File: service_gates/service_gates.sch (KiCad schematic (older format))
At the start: 1 part, among them P1 DIN_41612_128P

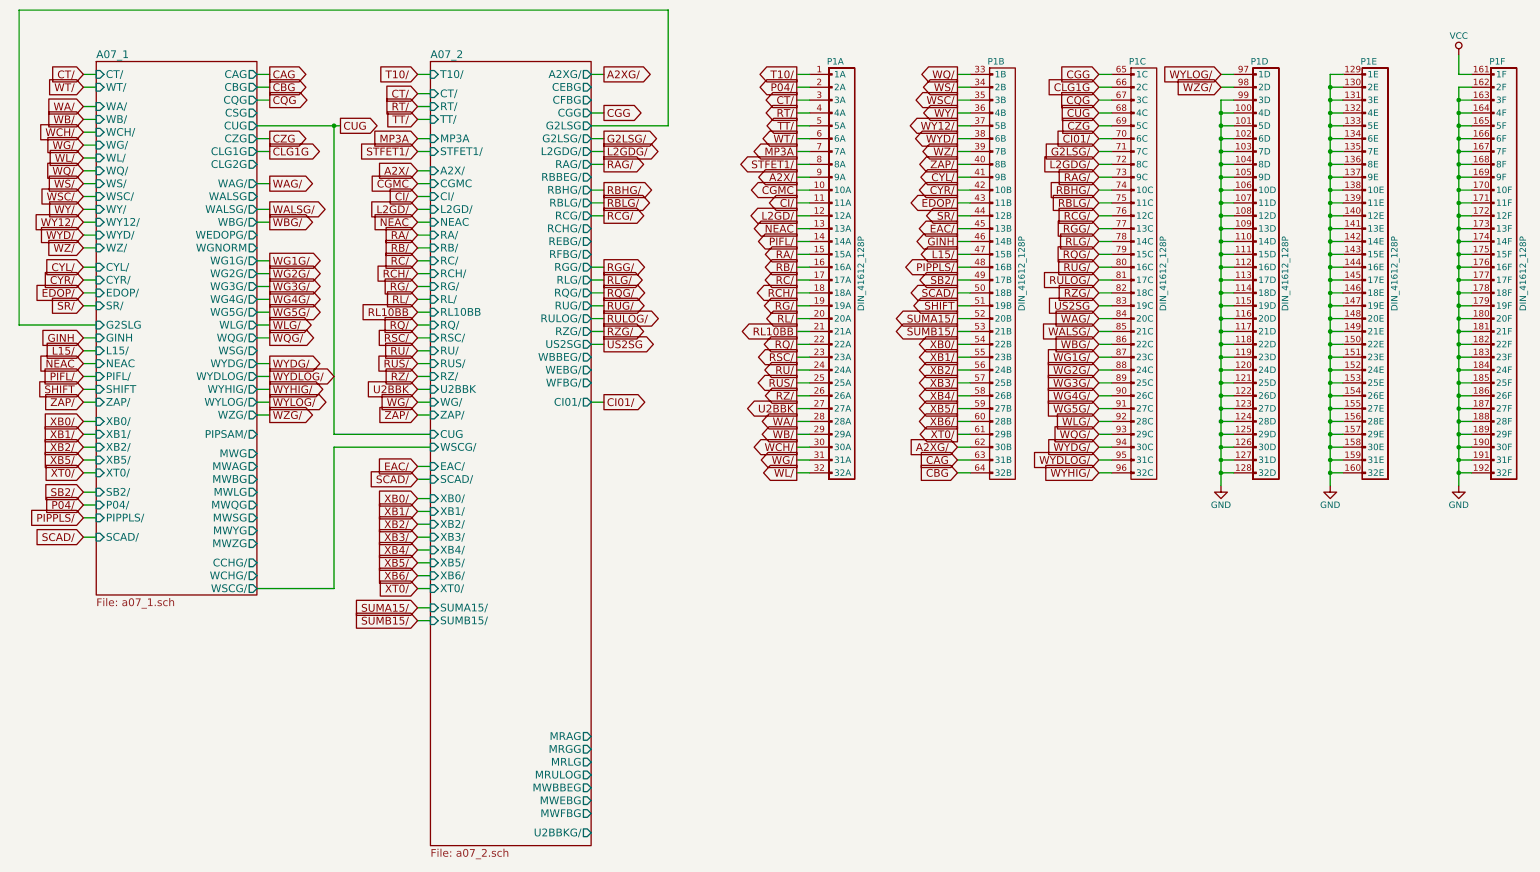
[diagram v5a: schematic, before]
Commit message: Added and tied in module 12, parity & s register
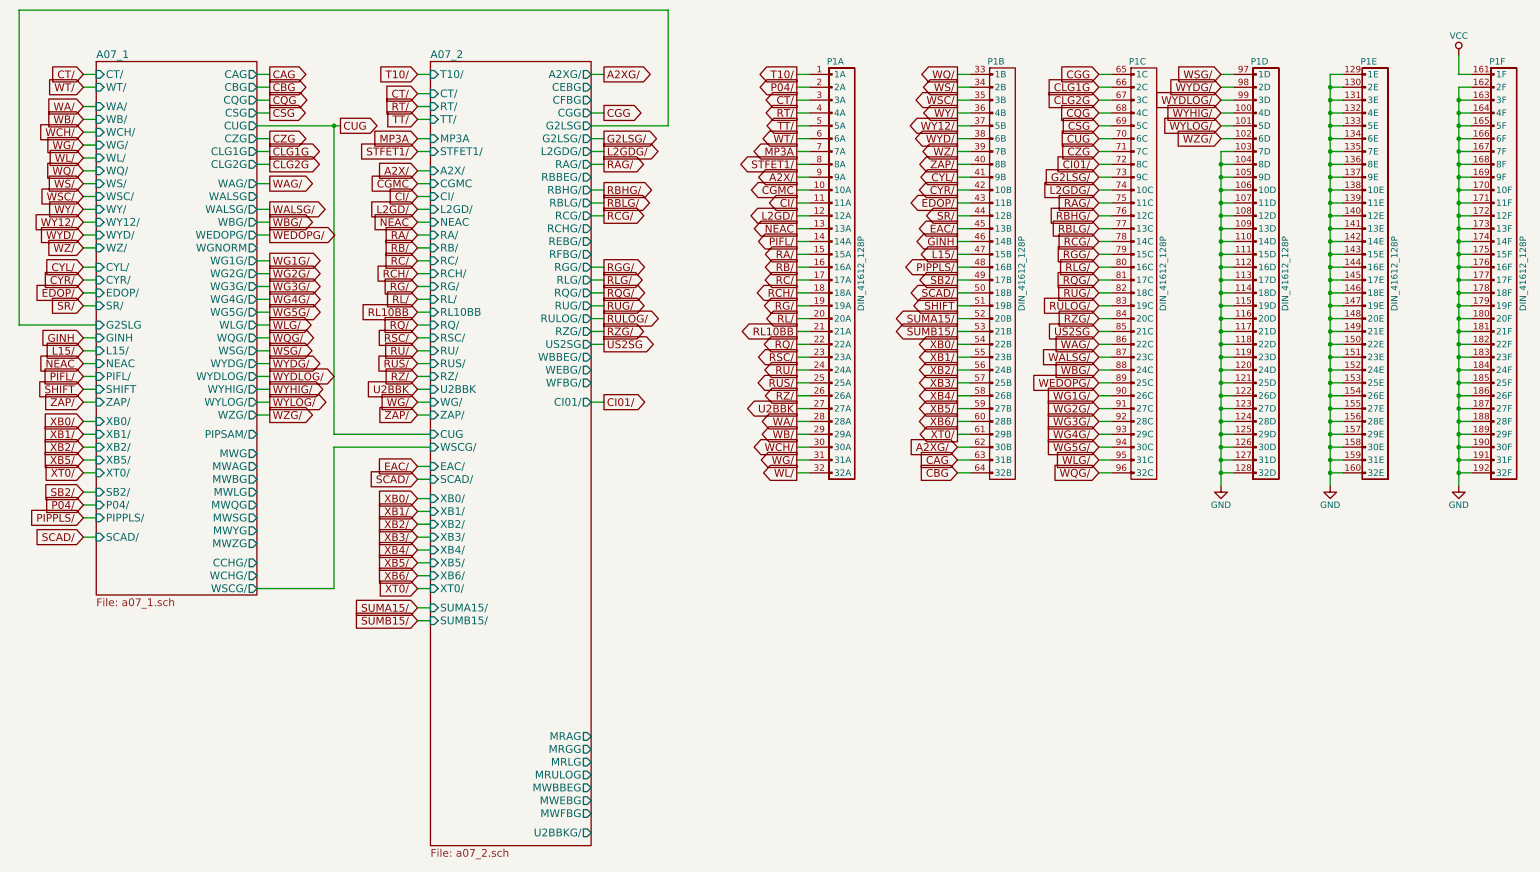
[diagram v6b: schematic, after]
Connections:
- net CI01/: now also P1.72 (8C); no longer P1.70 (6C)
- net CQG: now also P1.68 (4C); no longer P1.67 (3C)
- net CUG: now also P1.70 (6C); no longer P1.68 (4C)
- net CZG: now also P1.71 (7C); no longer P1.69 (5C)
- net G2LSG/: now also P1.73 (9C); no longer P1.71 (7C)
- net GND: no longer P1.100 (4D), P1.101 (5D), P1.102 (6D), P1.99 (3D)
- net L2GDG/: now also P1.74 (10C); no longer P1.72 (8C)
- net RAG/: now also P1.75 (11C); no longer P1.73 (9C)
- net RBHG/: now also P1.76 (12C); no longer P1.74 (10C)
- net RBLG/: now also P1.77 (13C); no longer P1.75 (11C)
- net RCG/: now also P1.78 (14C); no longer P1.76 (12C)
- net RGG/: now also P1.79 (15C); no longer P1.77 (13C)
- net RLG/: now also P1.80 (16C); no longer P1.78 (14C)
- net RQG/: now also P1.81 (17C); no longer P1.79 (15C)
- net RUG/: now also P1.82 (18C); no longer P1.80 (16C)
- net RULOG/: now also P1.83 (19C); no longer P1.81 (17C)
- net RZG/: now also P1.84 (20C); no longer P1.82 (18C)
- net US2SG: now also P1.85 (21C); no longer P1.83 (19C)
- net WAG/: now also P1.86 (22C); no longer P1.84 (20C)
- net WALSG/: now also P1.87 (23C); no longer P1.85 (21C)
- net WBG/: now also P1.88 (24C); no longer P1.86 (22C)
- net WG1G/: now also P1.90 (26C); no longer P1.87 (23C)
- net WG2G/: now also P1.91 (27C); no longer P1.88 (24C)
- net WG3G/: now also P1.92 (28C); no longer P1.89 (25C)
- net WG4G/: now also P1.93 (29C); no longer P1.90 (26C)
- net WG5G/: now also P1.94 (30C); no longer P1.91 (27C)
- net WLG/: now also P1.95 (31C); no longer P1.92 (28C)
- net WQG/: now also P1.96 (32C); no longer P1.93 (29C)
- net WYDG/: now also P1.98 (2D); no longer P1.94 (30C)
- net WYDLOG/: now also P1.99 (3D); no longer P1.95 (31C)
- net WYHIG/: now also P1.100 (4D); no longer P1.96 (32C)
- net WYLOG/: now also P1.101 (5D); no longer P1.97 (1D)
- net WZG/: now also P1.102 (6D); no longer P1.98 (2D)
- new net CLG2G: P1.67 (3C)
- new net CSG: P1.69 (5C)
- new net WEDOPG/: P1.89 (25C)
- new net WSG/: P1.97 (1D)
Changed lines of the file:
@@
 $EndComp
 Wire Wire Line
-	11550 1450 11650 1450
-Wire Wire Line
-	10600 3050 10700 3050
+	11550 1850 11650 1850
+Wire Wire Line
+	10600 3250 10700 3250
+Wire Wire Line
+	10600 2950 10700 2950
+Wire Wire Line
+	10600 2850 10700 2850
 Wire Wire Line
 	10600 2750 10700 2750
 Wire Wire Line
 	10600 2650 10700 2650
-Wire Wire Line
-	10600 2550 10700 2550
-Wire Wire Line
-	10600 2450 10700 2450
 $Comp
 L DIN_41612_128P P1
@@
 	11550 1950 11650 1950
 Connection ~ 11550 2050
-Wire Wire Line
-	11550 1850 11650 1850
-Connection ~ 11550 1950
-Wire Wire Line
-	11550 1750 11650 1750
-Connection ~ 11550 1850
-Wire Wire Line
-	11550 1650 11650 1650
-Connection ~ 11550 1750
-Wire Wire Line
-	11550 1550 11650 1550
-Connection ~ 11550 1650
 $Comp
 L DIN_41612_128P P1
@@
 Connection ~ 12400 1450
 Wire Wire Line
-	10600 1850 10700 1850
+	10600 2050 10700 2050
 $Sheet
 S 5400 1250 1250 6100
@@
 Connection ~ 4650 1750
 Wire Wire Line
-	10700 1550 10600 1550
-Text GLabel 10600 1550 0    60   Input ~ 0
-CQG
-Wire Wire Line
 	10700 1650 10600 1650
 Text GLabel 10600 1650 0    60   Input ~ 0
+CQG
+Wire Wire Line
+	10700 1850 10600 1850
+Text GLabel 10600 1850 0    60   Input ~ 0
 CUG
 Wire Wire Line
@@
 CZG
 Wire Wire Line
-	10700 1750 10600 1750
-Text GLabel 10600 1750 0    60   Input ~ 0
+	10700 1950 10600 1950
+Text GLabel 10600 1950 0    60   Input ~ 0
 CZG
 Wire Wire Line
@@
 Text GLabel 6750 3900 2    60   Output ~ 0
 CI01/
-Text GLabel 10600 1850 0    60   Input ~ 0
+Text GLabel 10600 2050 0    60   Input ~ 0
 CI01/
 Wire Wire Line
@@
 G2LSG/
 Wire Wire Line
-	10600 1950 10700 1950
-Text GLabel 10600 1950 0    60   Input ~ 0
+	10600 2150 10700 2150
+Text GLabel 10600 2150 0    60   Input ~ 0
 G2LSG/
 Wire Wire Line
@@
 L2GDG/
 Wire Wire Line
-	10600 2050 10700 2050
-Text GLabel 10600 2050 0    60   Input ~ 0
+	10600 2250 10700 2250
+Text GLabel 10600 2250 0    60   Input ~ 0
 L2GDG/
 Wire Wire Line
@@
 RAG/
 Wire Wire Line
-	10600 2150 10700 2150
-Text GLabel 10600 2150 0    60   Input ~ 0
+	10600 2350 10700 2350
+Text GLabel 10600 2350 0    60   Input ~ 0
 RAG/
 Wire Wire Line
@@
 RBLG/
 Wire Wire Line
-	10600 2350 10700 2350
-Text GLabel 10600 2350 0    60   Input ~ 0
+	10600 2550 10700 2550
+Text GLabel 10600 2550 0    60   Input ~ 0
 RBLG/
 Wire Wire Line
@@
 Text GLabel 6750 2450 2    60   Output ~ 0
 RCG/
-Text GLabel 10600 2450 0    60   Input ~ 0
+Text GLabel 10600 2650 0    60   Input ~ 0
 RCG/
 Wire Wire Line
@@
 Text GLabel 6750 2850 2    60   Output ~ 0
 RGG/
-Text GLabel 10600 2550 0    60   Input ~ 0
+Text GLabel 10600 2750 0    60   Input ~ 0
 RGG/
 Wire Wire Line
@@
 Text GLabel 6750 2950 2    60   Output ~ 0
 RLG/
-Text GLabel 10600 2650 0    60   Input ~ 0
+Text GLabel 10600 2850 0    60   Input ~ 0
 RLG/
 Wire Wire Line
@@
 Text GLabel 6750 3050 2    60   Output ~ 0
 RQG/
-Text GLabel 10600 2750 0    60   Input ~ 0
+Text GLabel 10600 2950 0    60   Input ~ 0
 RQG/
 Wire Wire Line
@@
 RULOG/
 Wire Wire Line
-	10600 2950 10700 2950
-Text GLabel 10600 2950 0    60   Input ~ 0
+	10600 3150 10700 3150
+Text GLabel 10600 3150 0    60   Input ~ 0
 RULOG/
 Wire Wire Line
@@
 Text GLabel 6750 3350 2    60   Output ~ 0
 RZG/
-Text GLabel 10600 3050 0    60   Input ~ 0
+Text GLabel 10600 3250 0    60   Input ~ 0
 RZG/
 Wire Wire Line
@@
 WALSG/
 Wire Wire Line
-	10600 3250 10700 3250
-Text GLabel 10600 3250 0    60   Input ~ 0
+	10600 3450 10700 3450
+Text GLabel 10600 3450 0    60   Input ~ 0
 WAG/
 Wire Wire Line
-	10600 3350 10700 3350
-Text GLabel 10600 3350 0    60   Input ~ 0
+	10600 3550 10700 3550
+Text GLabel 10600 3550 0    60   Input ~ 0
 WALSG/
 Wire Wire Line
@@
 WBG/
 Wire Wire Line
-	10600 3450 10700 3450
-Text GLabel 10600 3450 0    60   Input ~ 0
+	10600 3650 10700 3650
+Text GLabel 10600 3650 0    60   Input ~ 0
 WBG/
 Wire Wire Line
@@
 WG4G/
 Wire Wire Line
-	10600 3550 10700 3550
-Text GLabel 10600 3550 0    60   Input ~ 0
-WG1G/
-Wire Wire Line
-	10600 3750 10700 3750
-Text GLabel 10600 3750 0    60   Input ~ 0
-WG3G/
-Wire Wire Line
 	10600 3850 10700 3850
 Text GLabel 10600 3850 0    60   Input ~ 0
+WG1G/
+Wire Wire Line
+	10600 4050 10700 4050
+Text GLabel 10600 4050 0    60   Input ~ 0
+WG3G/
+Wire Wire Line
+	10600 4150 10700 4150
+Text GLabel 10600 4150 0    60   Input ~ 0
 WG4G/
 Wire Wire Line
@@
 WLG/
 Wire Wire Line
-	10600 4050 10700 4050
-Text GLabel 10600 4050 0    60   Input ~ 0
+	10600 4350 10700 4350
+Text GLabel 10600 4350 0    60   Input ~ 0
 WLG/
 Wire Wire Line
-	10600 4150 10700 4150
-Text GLabel 10600 4150 0    60   Input ~ 0
+	10600 4450 10700 4450
+Text GLabel 10600 4450 0    60   Input ~ 0
 WQG/
 Wire Wire Line
@@
 WYLOG/
 Wire Wire Line
-	10600 4250 10700 4250
-Text GLabel 10600 4250 0    60   Input ~ 0
+	11550 1450 11650 1450
+Text GLabel 11550 1450 0    60   Input ~ 0
 WYDG/
 Wire Wire Line
-	10600 4350 10700 4350
-Text GLabel 10600 4350 0    60   Input ~ 0
+	11550 1550 11650 1550
+Text GLabel 11550 1550 0    60   Input ~ 0
 WYDLOG/
 Wire Wire Line
-	11550 1350 11650 1350
-Text GLabel 11550 1350 0    60   Input ~ 0
+	11550 1750 11650 1750
+Text GLabel 11550 1750 0    60   Input ~ 0
 WYLOG/
 Wire Wire Line
@@
 Text GLabel 4150 4000 2    60   Output ~ 0
 WZG/
-Text GLabel 11550 1450 0    60   Input ~ 0
+Text GLabel 11550 1850 0    60   Input ~ 0
 WZG/
 Wire Wire Line
@@
 RBHG/
 Wire Wire Line
-	10600 2250 10700 2250
-Text GLabel 10600 2250 0    60   Input ~ 0
+	10600 2450 10700 2450
+Text GLabel 10600 2450 0    60   Input ~ 0
 RBHG/
 Wire Wire Line
@@
 RUG/
 Wire Wire Line
-	10600 2850 10700 2850
-Text GLabel 10600 2850 0    60   Input ~ 0
+	10600 3050 10700 3050
+Text GLabel 10600 3050 0    60   Input ~ 0
 RUG/
 Wire Wire Line
@@
 WG5G/
 Wire Wire Line
-	10600 3650 10700 3650
-Text GLabel 10600 3650 0    60   Input ~ 0
-WG2G/
-Wire Wire Line
 	10600 3950 10700 3950
 Text GLabel 10600 3950 0    60   Input ~ 0
+WG2G/
+Wire Wire Line
+	10600 4250 10700 4250
+Text GLabel 10600 4250 0    60   Input ~ 0
 WG5G/
 Wire Wire Line
@@
 WYHIG/
 Wire Wire Line
-	10600 4450 10700 4450
-Text GLabel 10600 4450 0    60   Input ~ 0
+	11550 1650 11650 1650
+Text GLabel 11550 1650 0    60   Input ~ 0
 WYHIG/
 Wire Wire Line
@@
 SUMB15/
 Wire Wire Line
-	11550 1550 11550 4550
-Wire Wire Line
-	10600 3150 10700 3150
-Text GLabel 10600 3150 0    60   Input ~ 0
+	10600 3350 10700 3350
+Text GLabel 10600 3350 0    60   Input ~ 0
 US2SG
 Wire Wire Line
@@
 Text GLabel 9500 3350 0    60   Output ~ 0
 SUMB15/
+Wire Wire Line
+	4050 1650 4150 1650
+Text GLabel 4150 1650 2    60   Output ~ 0
+CSG
+Wire Wire Line
+	10700 1750 10600 1750
+Text GLabel 10600 1750 0    60   Input ~ 0
+CSG
+Wire Wire Line
+	4050 3500 4150 3500
+Text GLabel 4150 3500 2    60   Output ~ 0
+WSG/
+Wire Wire Line
+	11550 1350 11650 1350
+Text GLabel 11550 1350 0    60   Input ~ 0
+WSG/
+Wire Wire Line
+	4050 2600 4150 2600
+Text GLabel 4150 2600 2    60   Output ~ 0
+WEDOPG/
+Wire Wire Line
+	10600 3750 10700 3750
+Text GLabel 10600 3750 0    60   Input ~ 0
+WEDOPG/
+Wire Wire Line
+	11550 1950 11550 4550
+Wire Wire Line
+	4050 2050 4150 2050
+Text GLabel 4150 2050 2    60   Output ~ 0
+CLG2G
+Wire Wire Line
+	10700 1550 10600 1550
+Text GLabel 10600 1550 0    60   Input ~ 0
+CLG2G
 $EndSCHEMATC

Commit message: Added and tied in module 15, the rupt service (and banking/rope+strand selection)
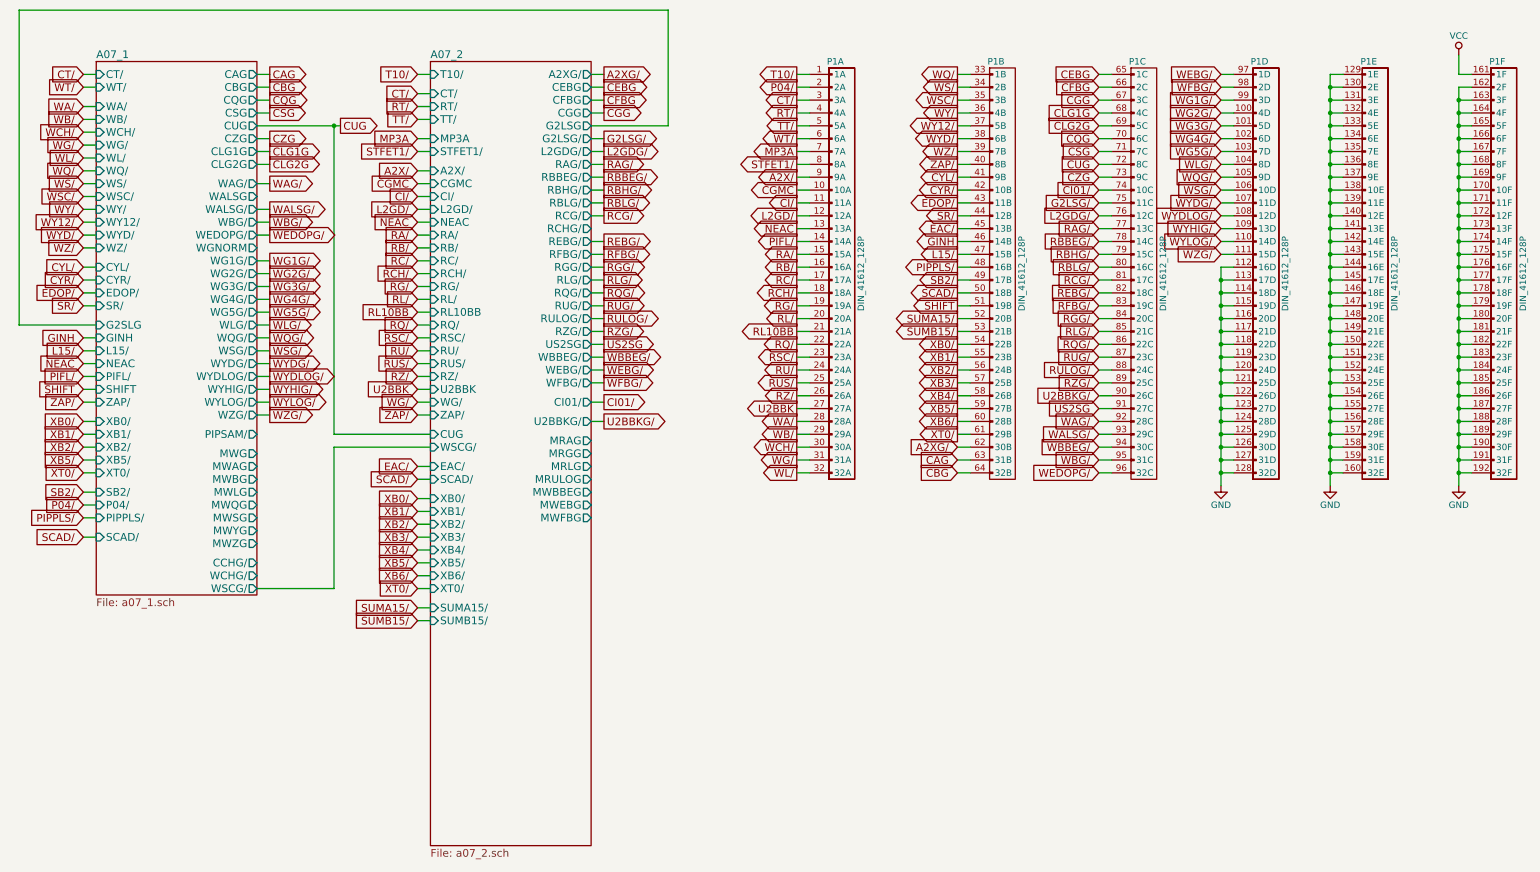
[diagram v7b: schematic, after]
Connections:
- net CGG: now also P1.67 (3C); no longer P1.65 (1C)
- net CI01/: now also P1.74 (10C); no longer P1.72 (8C)
- net CLG1G: now also P1.68 (4C); no longer P1.66 (2C)
- net CLG2G: now also P1.69 (5C); no longer P1.67 (3C)
- net CQG: now also P1.70 (6C); no longer P1.68 (4C)
- net CSG: now also P1.71 (7C); no longer P1.69 (5C)
- net CUG: now also P1.72 (8C); no longer P1.70 (6C)
- net CZG: now also P1.73 (9C); no longer P1.71 (7C)
- net G2LSG/: now also P1.75 (11C); no longer P1.73 (9C)
- net GND: no longer P1.103 (7D), P1.104 (8D), P1.105 (9D), P1.106 (10D), P1.107 (11D), P1.108 (12D), P1.109 (13D), P1.110 (14D), P1.111 (15D)
- net L2GDG/: now also P1.76 (12C); no longer P1.74 (10C)
- net RAG/: now also P1.77 (13C); no longer P1.75 (11C)
- net RBHG/: now also P1.79 (15C); no longer P1.76 (12C)
- net RBLG/: now also P1.80 (16C); no longer P1.77 (13C)
- net RCG/: now also P1.81 (17C); no longer P1.78 (14C)
- net RGG/: now also P1.84 (20C); no longer P1.79 (15C)
- net RLG/: now also P1.85 (21C); no longer P1.80 (16C)
- net RQG/: now also P1.86 (22C); no longer P1.81 (17C)
- net RUG/: now also P1.87 (23C); no longer P1.82 (18C)
- net RULOG/: now also P1.88 (24C); no longer P1.83 (19C)
- net RZG/: now also P1.89 (25C); no longer P1.84 (20C)
- net US2SG: now also P1.91 (27C); no longer P1.85 (21C)
- net WAG/: now also P1.92 (28C); no longer P1.86 (22C)
- net WALSG/: now also P1.93 (29C); no longer P1.87 (23C)
- net WBG/: now also P1.95 (31C); no longer P1.88 (24C)
- net WEDOPG/: now also P1.96 (32C); no longer P1.89 (25C)
- net WG1G/: now also P1.99 (3D); no longer P1.90 (26C)
- net WG2G/: now also P1.100 (4D); no longer P1.91 (27C)
- net WG3G/: now also P1.101 (5D); no longer P1.92 (28C)
- net WG4G/: now also P1.102 (6D); no longer P1.93 (29C)
- net WG5G/: now also P1.103 (7D); no longer P1.94 (30C)
- net WLG/: now also P1.104 (8D); no longer P1.95 (31C)
- net WQG/: now also P1.105 (9D); no longer P1.96 (32C)
- net WSG/: now also P1.106 (10D); no longer P1.97 (1D)
- net WYDG/: now also P1.107 (11D); no longer P1.98 (2D)
- net WYDLOG/: now also P1.108 (12D); no longer P1.99 (3D)
- net WYHIG/: now also P1.109 (13D); no longer P1.100 (4D)
- net WYLOG/: now also P1.110 (14D); no longer P1.101 (5D)
- net WZG/: now also P1.111 (15D); no longer P1.102 (6D)
- new net CEBG: P1.65 (1C)
- new net CFBG: P1.66 (2C)
- new net RBBEG/: P1.78 (14C)
- new net REBG/: P1.82 (18C)
- new net RFBG/: P1.83 (19C)
- new net U2BBKG/: P1.90 (26C)
- new net WBBEG/: P1.94 (30C)
- new net WEBG/: P1.97 (1D)
- new net WFBG/: P1.98 (2D)
